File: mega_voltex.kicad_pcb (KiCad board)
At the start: 2 copper layers, 8 parts, among them J1 Arduino_Mega_Header

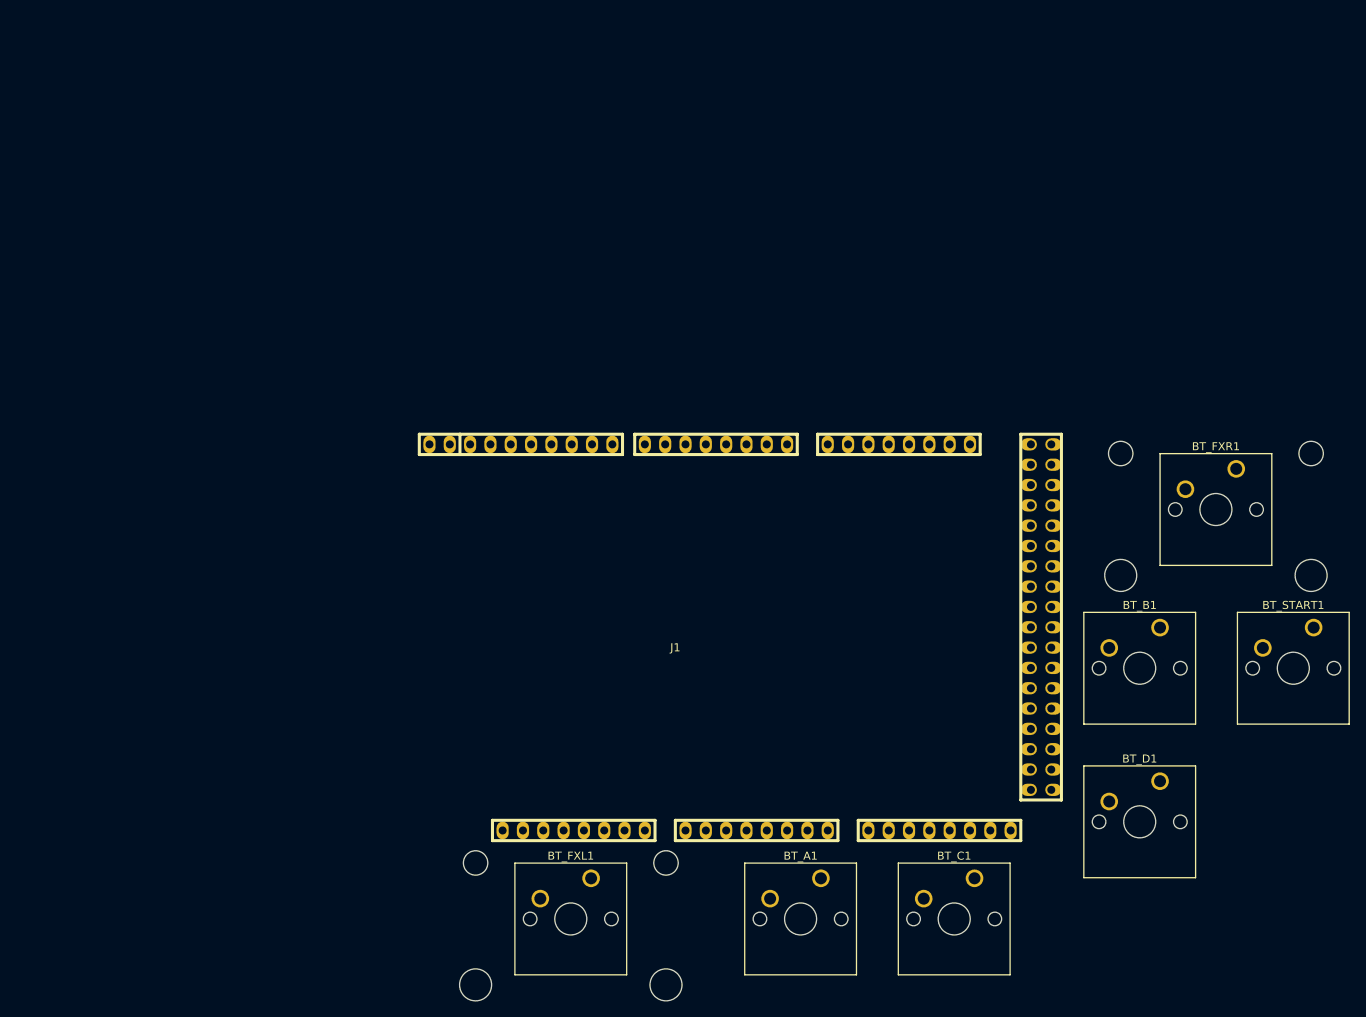
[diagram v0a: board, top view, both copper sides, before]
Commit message: Rearranged board, renamed module
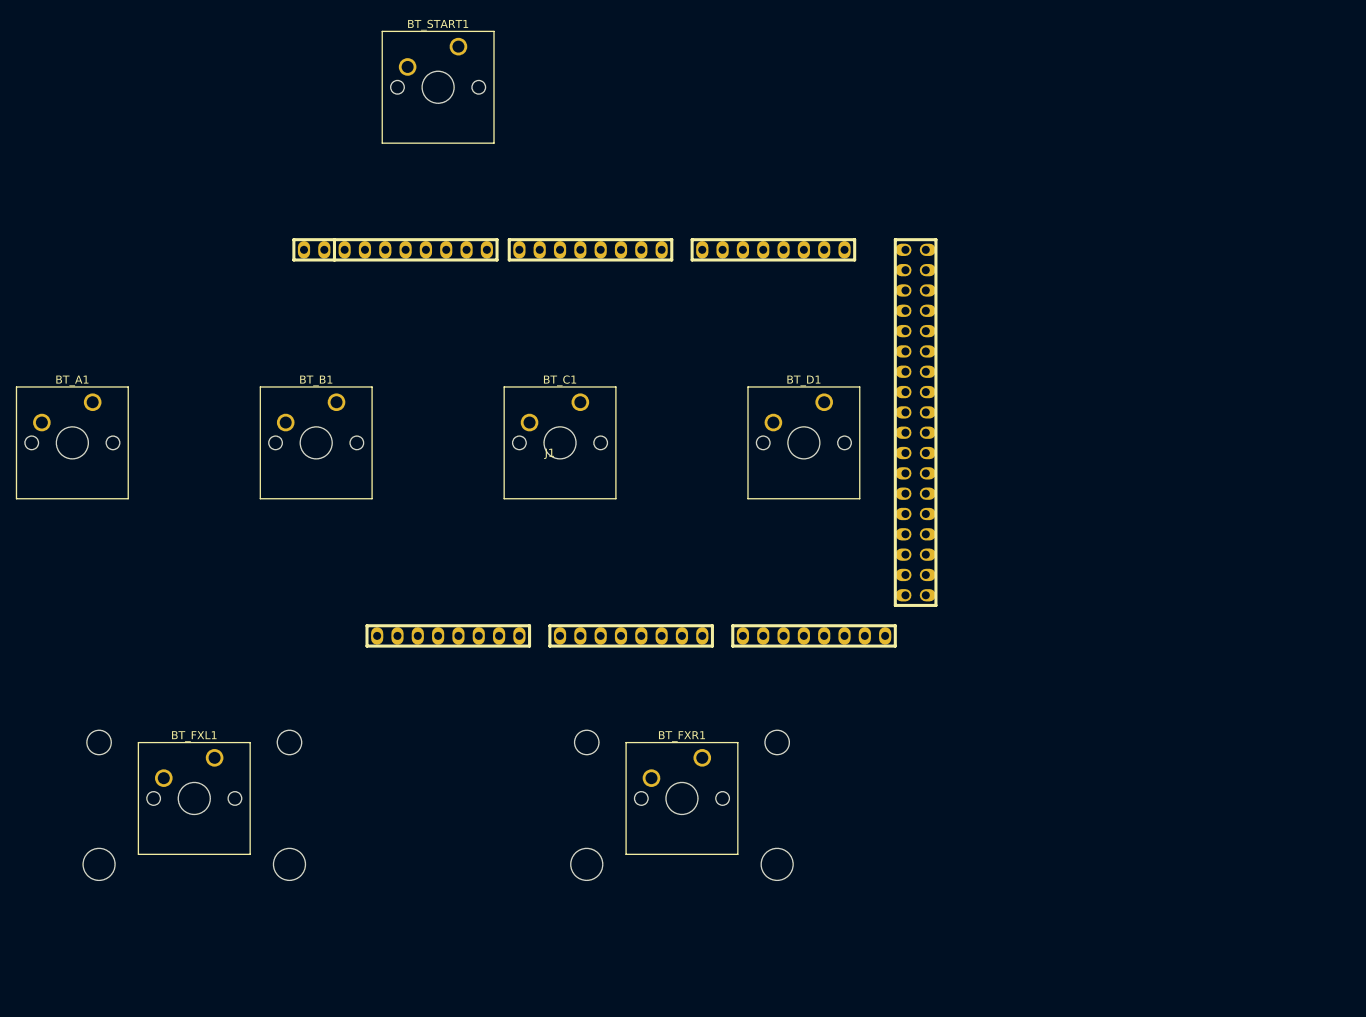
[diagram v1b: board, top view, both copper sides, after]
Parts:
- moved BT_START1 129.2 mm to (134.6, 33.0)
- moved BT_A1 108.8 mm to (88.9, 77.5)
- moved BT_B1 106.7 mm to (119.4, 77.5)
- moved BT_C1 77.3 mm to (149.9, 77.5)
- moved BT_FXR1 75.9 mm to (165.1, 121.9)
- moved BT_D1 63.3 mm to (180.3, 77.5)
- moved BT_FXL1 49.4 mm to (104.1, 121.9)
- moved J1 28.9 mm to (146.1, 82.5)
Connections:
- BT_A1 pad 1: Net-(BT_A1-Pad1) -> BT_A
- BT_B1 pad 1: Net-(BT_B1-Pad1) -> BT_B
- BT_C1 pad 1: Net-(BT_C1-Pad1) -> BT_C
- BT_D1 pad 1: Net-(BT_D1-Pad1) -> BT_D
- BT_FXL1 pad 1: Net-(BT_FXL1-Pad1) -> BT_FXL
- BT_FXR1 pad 1: Net-(BT_FXR1-Pad1) -> BT_FXR
- BT_START1 pad 1: Net-(BT_START1-Pad1) -> BT_START
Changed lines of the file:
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@@
-(kicad_pcb (version 20171130) (host pcbnew 5.0.0+dfsg1-2)
+(kicad_pcb (version 20171130) (host pcbnew 5.0.1)
   (general
     (thickness 1.6)
@@
     (zones 0)
     (modules 8)
-    (nets 93)
+    (nets 86)
   )
   (page A4)
@@
     (45 Margin user)
     (46 B.CrtYd user)
-    (47 F.CrtYd user)
+    (47 F.CrtYd user hide)
     (48 B.Fab user)
-    (49 F.Fab user)
+    (49 F.Fab user hide)
   )
   (setup
@@
   (net 84 "Net-(J1-Pad3)")
   (net 85 "Net-(J1-Pad2)")
-  (net 86 "Net-(BT_A1-Pad1)")
-  (net 87 "Net-(BT_B1-Pad1)")
-  (net 88 "Net-(BT_C1-Pad1)")
-  (net 89 "Net-(BT_D1-Pad1)")
-  (net 90 "Net-(BT_FXL1-Pad1)")
-  (net 91 "Net-(BT_FXR1-Pad1)")
-  (net 92 "Net-(BT_START1-Pad1)")
   (net_class Default "This is the default net class."
     (clearance 0.2)
@@
     (add_net LT_FXR)
     (add_net LT_START)
-    (add_net "Net-(BT_A1-Pad1)")
-    (add_net "Net-(BT_B1-Pad1)")
-    (add_net "Net-(BT_C1-Pad1)")
-    (add_net "Net-(BT_D1-Pad1)")
-    (add_net "Net-(BT_FXL1-Pad1)")
-    (add_net "Net-(BT_FXR1-Pad1)")
-    (add_net "Net-(BT_START1-Pad1)")
     (add_net "Net-(J1-Pad15)")
     (add_net "Net-(J1-Pad16)")
@@
   )
   (module Button_Switch_Keyboard:SW_Cherry_MX1A_1.00u_PCB (layer F.Cu)
-    (at 179.930001 136.980001)
+    (at 88.9 77.47)
     (descr "Cherry MX keyswitch, MX1A, 1.00u, PCB mount, http://cherryamericas.com/wp-content/uploads/2014/12/mx_cat.pdf")
     (tags "cherry mx keyswitch MX1A 1.00u PCB")
@@
     (fp_line (start -9.525 12.065) (end -9.525 -1.905) (layer F.SilkS) (width 0.12))
     (pad 1 thru_hole circle (at 0 0) (size 2.2 2.2) (drill 1.5) (layers *.Cu *.Mask)
-      (net 86 "Net-(BT_A1-Pad1)"))
+      (net 76 BT_A))
     (pad 2 thru_hole circle (at -6.35 2.54) (size 2.2 2.2) (drill 1.5) (layers *.Cu *.Mask)
       (net 44 GND))
@@
   )
   (module Button_Switch_Keyboard:SW_Cherry_MX1A_1.00u_PCB (layer F.Cu)
-    (at 222.320001 105.640001)
+    (at 119.38 77.47)
     (descr "Cherry MX keyswitch, MX1A, 1.00u, PCB mount, http://cherryamericas.com/wp-content/uploads/2014/12/mx_cat.pdf")
     (tags "cherry mx keyswitch MX1A 1.00u PCB")
@@
       (net 44 GND))
     (pad 1 thru_hole circle (at 0 0) (size 2.2 2.2) (drill 1.5) (layers *.Cu *.Mask)
-      (net 87 "Net-(BT_B1-Pad1)"))
+      (net 75 BT_B))
     (model ${KISYS3DMOD}/Button_Switch_Keyboard.3dshapes/SW_Cherry_MX1A_1.00u_PCB.wrl
       (at (xyz 0 0 0))
@@
   )
   (module Button_Switch_Keyboard:SW_Cherry_MX1A_1.00u_PCB (layer F.Cu)
-    (at 199.130001 136.980001)
+    (at 149.86 77.47)
     (descr "Cherry MX keyswitch, MX1A, 1.00u, PCB mount, http://cherryamericas.com/wp-content/uploads/2014/12/mx_cat.pdf")
     (tags "cherry mx keyswitch MX1A 1.00u PCB")
@@
     (fp_line (start -9.525 12.065) (end -9.525 -1.905) (layer F.SilkS) (width 0.12))
     (pad 1 thru_hole circle (at 0 0) (size 2.2 2.2) (drill 1.5) (layers *.Cu *.Mask)
-      (net 88 "Net-(BT_C1-Pad1)"))
+      (net 74 BT_C))
     (pad 2 thru_hole circle (at -6.35 2.54) (size 2.2 2.2) (drill 1.5) (layers *.Cu *.Mask)
       (net 44 GND))
@@
   )
   (module Button_Switch_Keyboard:SW_Cherry_MX1A_1.00u_PCB (layer F.Cu)
-    (at 222.320001 124.840001)
+    (at 180.34 77.47)
     (descr "Cherry MX keyswitch, MX1A, 1.00u, PCB mount, http://cherryamericas.com/wp-content/uploads/2014/12/mx_cat.pdf")
     (tags "cherry mx keyswitch MX1A 1.00u PCB")
@@
       (net 44 GND))
     (pad 1 thru_hole circle (at 0 0) (size 2.2 2.2) (drill 1.5) (layers *.Cu *.Mask)
-      (net 89 "Net-(BT_D1-Pad1)"))
+      (net 73 BT_D))
     (model ${KISYS3DMOD}/Button_Switch_Keyboard.3dshapes/SW_Cherry_MX1A_1.00u_PCB.wrl
       (at (xyz 0 0 0))
@@
   )
   (module Button_Switch_Keyboard:SW_Cherry_MX1A_2.00u_PCB (layer F.Cu)
-    (at 151.205001 136.980001)
+    (at 104.14 121.92)
     (descr "Cherry MX keyswitch, MX1A, 2.00u, PCB mount, http://cherryamericas.com/wp-content/uploads/2014/12/mx_cat.pdf")
     (tags "cherry mx keyswitch MX1A 2.00u PCB")
@@
     (fp_line (start -9.525 12.065) (end -9.525 -1.905) (layer F.SilkS) (width 0.12))
     (pad 1 thru_hole circle (at 0 0) (size 2.2 2.2) (drill 1.5) (layers *.Cu *.Mask)
-      (net 90 "Net-(BT_FXL1-Pad1)"))
+      (net 77 BT_FXL))
     (pad 2 thru_hole circle (at -6.35 2.54) (size 2.2 2.2) (drill 1.5) (layers *.Cu *.Mask)
       (net 44 GND))
@@
   )
   (module Button_Switch_Keyboard:SW_Cherry_MX1A_2.00u_PCB (layer F.Cu)
-    (at 231.845001 85.800001)
+    (at 165.1 121.92)
     (descr "Cherry MX keyswitch, MX1A, 2.00u, PCB mount, http://cherryamericas.com/wp-content/uploads/2014/12/mx_cat.pdf")
     (tags "cherry mx keyswitch MX1A 2.00u PCB")
@@
       (net 44 GND))
     (pad 1 thru_hole circle (at 0 0) (size 2.2 2.2) (drill 1.5) (layers *.Cu *.Mask)
-      (net 91 "Net-(BT_FXR1-Pad1)"))
+      (net 78 BT_FXR))
     (model ${KISYS3DMOD}/Button_Switch_Keyboard.3dshapes/SW_Cherry_MX1A_2.00u_PCB.wrl
       (at (xyz 0 0 0))
@@
   )
   (module Button_Switch_Keyboard:SW_Cherry_MX1A_1.00u_PCB (layer F.Cu)
-    (at 241.520001 105.640001)
+    (at 134.62 33.02)
     (descr "Cherry MX keyswitch, MX1A, 1.00u, PCB mount, http://cherryamericas.com/wp-content/uploads/2014/12/mx_cat.pdf")
     (tags "cherry mx keyswitch MX1A 1.00u PCB")
@@
     (fp_line (start -9.525 12.065) (end -9.525 -1.905) (layer F.SilkS) (width 0.12))
     (pad 1 thru_hole circle (at 0 0) (size 2.2 2.2) (drill 1.5) (layers *.Cu *.Mask)
-      (net 92 "Net-(BT_START1-Pad1)"))
+      (net 61 BT_START))
     (pad 2 thru_hole circle (at -6.35 2.54) (size 2.2 2.2) (drill 1.5) (layers *.Cu *.Mask)
       (net 44 GND))
@@
   )
   (module arduino_mega:arduino_mega_header (layer F.Cu)
-    (at 161.734501 106.870501)
+    (at 146.05 82.55)
     (descr "Arduino Mega/Due Header")
     (tags Arduino)

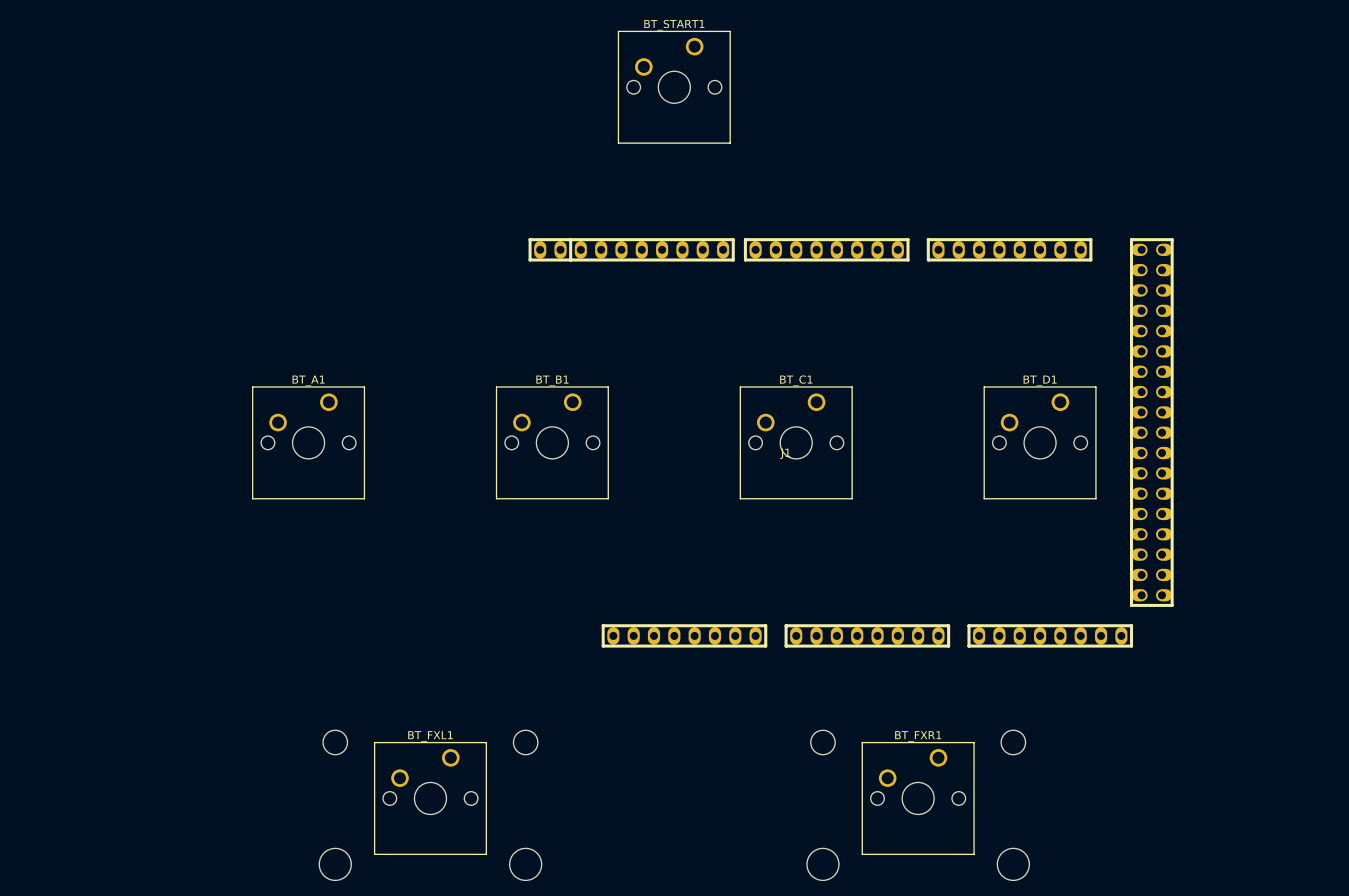
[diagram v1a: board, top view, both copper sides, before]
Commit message: Added new footprints, updated schematic & PCB
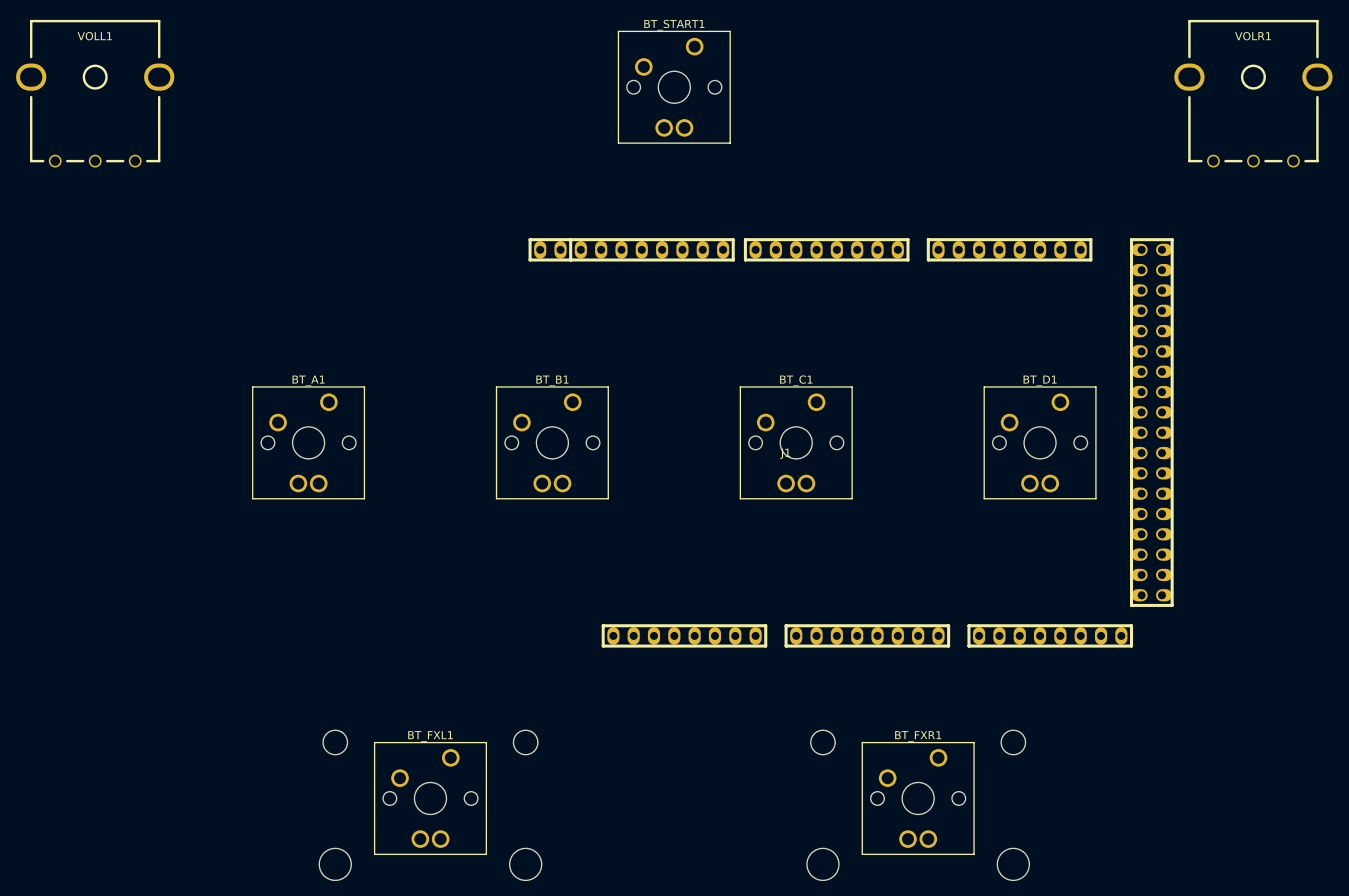
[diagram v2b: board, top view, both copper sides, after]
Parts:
- added VOLL1: Rotary_Encoder, mega_voltex:Encoder_Bourns_PEC16, F.Cu at (59.7, 36.8)
- added VOLR1: Rotary_Encoder, mega_voltex:Encoder_Bourns_PEC16, F.Cu at (204.5, 36.8)
- BT_A1, BT_B1, BT_C1, BT_D1, BT_START1: footprint Button_Switch_Keyboard:SW_Cherry_MX1A_1.00u_PCB -> mega_voltex:SW_Cherry_MX1A_1.00u_PCB
- BT_FXL1, BT_FXR1: footprint Button_Switch_Keyboard:SW_Cherry_MX1A_2.00u_PCB -> mega_voltex:SW_Cherry_MX1A_2.00u_PCB
- J1: footprint arduino_mega:arduino_mega_header -> mega_voltex:arduino_mega_header
